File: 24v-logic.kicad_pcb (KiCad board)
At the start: 2 copper layers, 56.4 x 78.7 mm, 55 parts, among them J1 Conn_02x10_Odd_Even, J2 Screw_Terminal_01x09, J3 Conn_02x10_Odd_Even

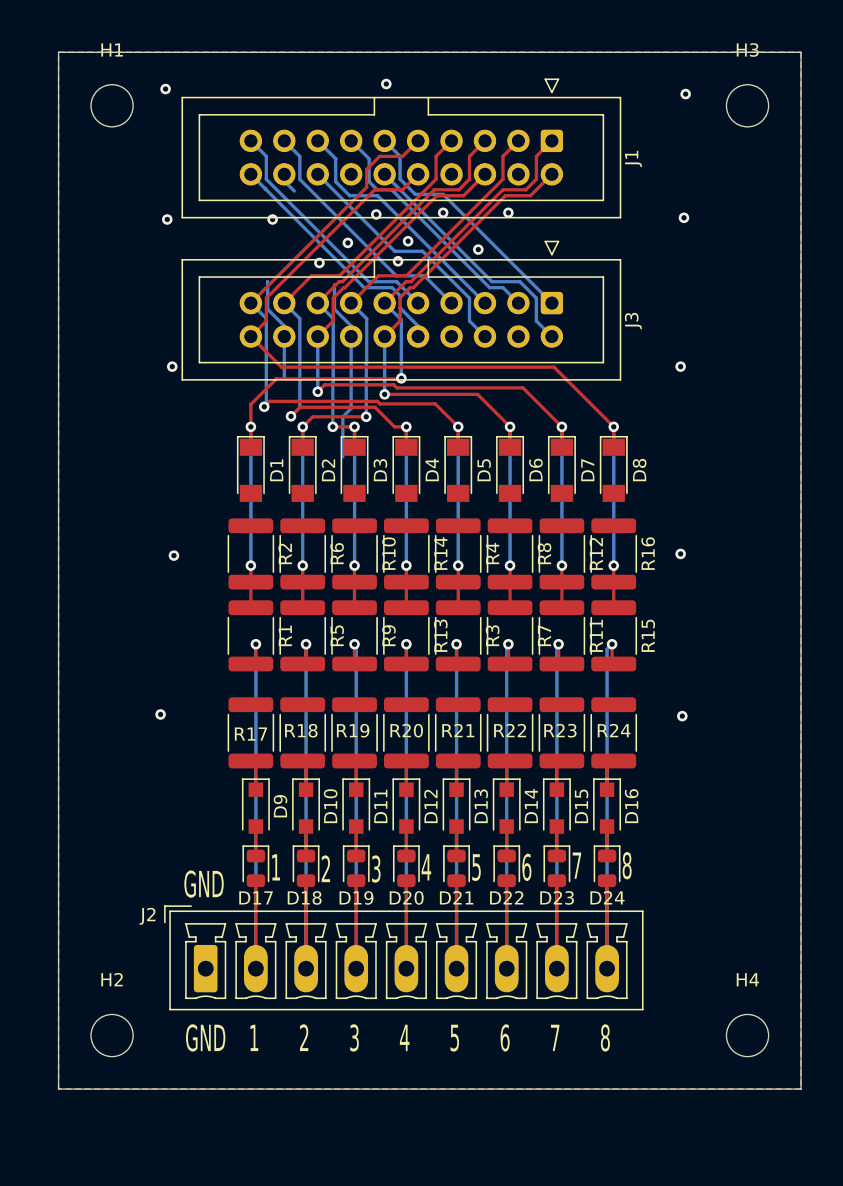
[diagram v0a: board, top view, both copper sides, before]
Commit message: Changes for missing components and migrating to KiCAD 6
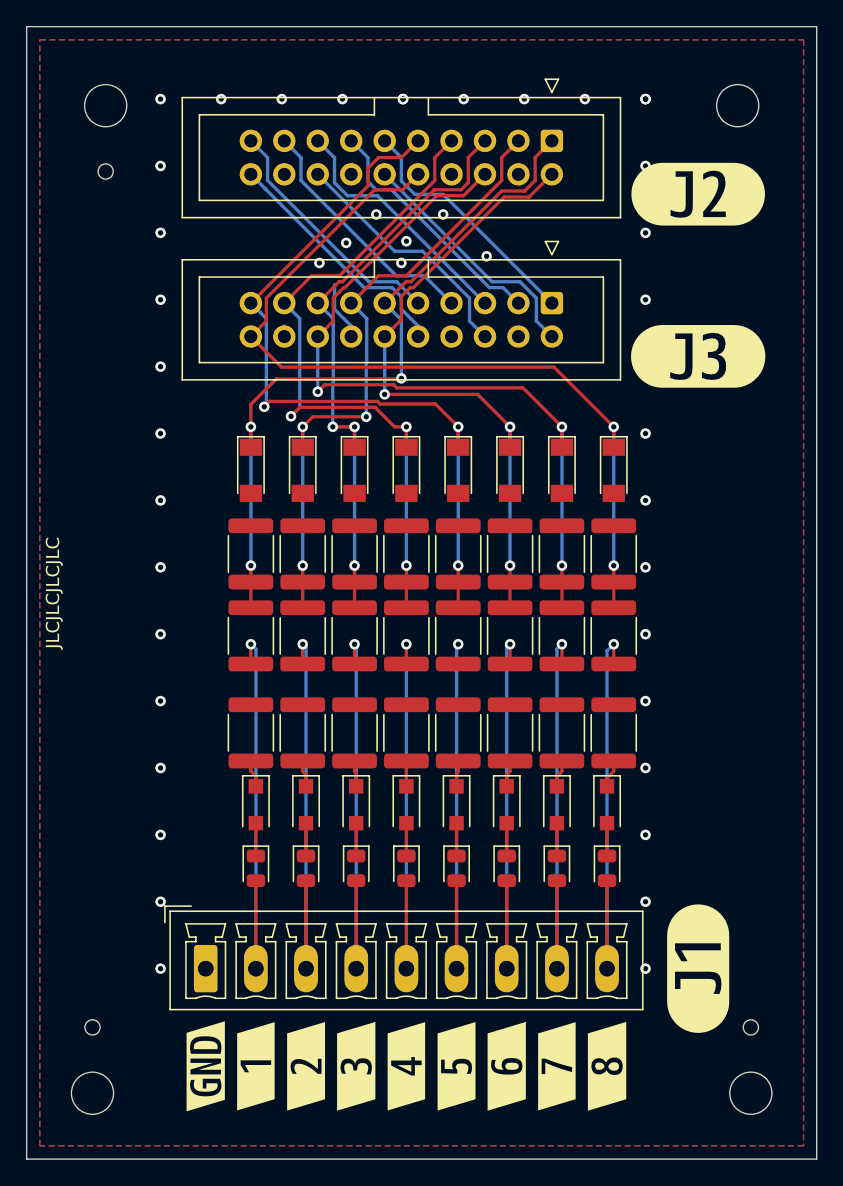
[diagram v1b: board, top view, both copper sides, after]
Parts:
- added REF**: MountingHole_2.1mm, MountingHole:MountingHole_2.1mm, F.Cu at (85.0, 134.0)
- added REF**: MountingHole_2.1mm, MountingHole:MountingHole_2.1mm, F.Cu at (135.0, 134.0)
- added REF**: MountingHole_2.1mm, MountingHole:MountingHole_2.1mm, F.Cu at (86.0, 69.0)
- added kibuzzard-62FC7920: G***, kibuzzard-62FC7920, F.Cu at (93.6, 137.0)
- added kibuzzard-62FC7940: G***, kibuzzard-62FC7940, F.Cu at (101.2, 137.0)
- added kibuzzard-62FC794D: G***, kibuzzard-62FC794D, F.Cu at (97.4, 137.0)
- added kibuzzard-62FC7992: G***, kibuzzard-62FC7992, F.Cu at (105.0, 137.0)
- added kibuzzard-62FC799A: G***, kibuzzard-62FC799A, F.Cu at (108.8, 137.0)
- added kibuzzard-62FC79A9: G***, kibuzzard-62FC79A9, F.Cu at (112.6, 137.0)
- added kibuzzard-62FC79AF: G***, kibuzzard-62FC79AF, F.Cu at (116.5, 137.0)
- added kibuzzard-62FC79B6: G***, kibuzzard-62FC79B6, F.Cu at (120.3, 137.0)
- added kibuzzard-62FC79BD: G***, kibuzzard-62FC79BD, F.Cu at (124.1, 137.0)
- added kibuzzard-62FC7CD0: G***, kibuzzard-62FC7CD0, F.Cu at (131.0, 129.5)
- added kibuzzard-62FC7D50: G***, kibuzzard-62FC7D50, F.Cu at (131.0, 83.0)
- added kibuzzard-62FC7D6D: G***, kibuzzard-62FC7D6D, F.Cu at (131.0, 70.7)
- D1, D3, D5, D7: value 5,6V -> D; footprint Diode_SMD:D_MiniMELF -> Diode_SMD:D_SOD-123F
- D10, D11, D14, D16: value D -> R; footprint Diode_SMD:D_SOD-123F -> Diode_SMD:D_0805_2012Metric
- D17, D18, D19, D20, D21, D22, D23, D24: value R -> 5,6V; footprint Diode_SMD:D_0805_2012Metric -> Diode_SMD:D_MiniMELF
- D2, D4, D6, D8: value 5,6V -> R; footprint Diode_SMD:D_MiniMELF -> Diode_SMD:D_0805_2012Metric
- R1, R19, R22, R5: value 3800 -> 1k
- R10, R14, R16, R2: value 1000 -> 1k
- R11, R13, R15, R17, R18, R20, R21, R23, R24, R3, R7, R9: value 3800 -> 3.9k
- R12, R4, R6, R8: value 1000 -> 3.9k
- moved D8 36.0 mm to (105.0, 121.9)
- moved D21 34.0 mm to (97.0, 91.7)
- moved D22 31.3 mm to (124.6, 91.7)
- moved D6 31.2 mm to (108.8, 121.9)
- moved D20 30.5 mm to (112.8, 91.7)
- moved D19 30.5 mm to (108.8, 91.7)
- moved D4 30.5 mm to (112.6, 121.9)
- moved D18 30.4 mm to (104.9, 91.7)
- moved D17 30.4 mm to (101.0, 91.7)
- moved D23 30.4 mm to (116.7, 91.7)
- moved D24 30.4 mm to (120.7, 91.7)
- moved D2 30.2 mm to (101.2, 121.9)
- moved D7 29.8 mm to (105.0, 117.1)
- moved R17 27.6 mm to (124.6, 111.6)
- moved R12 27.3 mm to (97.0, 111.6)
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- renumbered H2 to H1, H4 to H2, H1 to H3, H3 to H4, J2 to J1, J1 to J2
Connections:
- D1 pad 1: D0 -> Net-(D8-Pad1)
- D1 pad 2: GND -> Net-(D7-Pad1)
- D10 pad 1: Net-(D10-Pad1) -> Net-(D1-Pad1)
- D10 pad 2: Net-(D10-Pad2) -> I24-0
- D11 pad 1: Net-(D11-Pad1) -> Net-(D19-Pad1)
- D11 pad 2: Net-(D11-Pad2) -> I24-5
- D12 pad 2: Net-(D12-Pad2) -> Net-(D19-Pad1)
- D13 pad 1: Net-(D13-Pad1) -> Net-(D5-Pad1)
- D13 pad 2: Net-(D13-Pad2) -> Net-(D4-Pad1)
- D14 pad 1: Net-(D14-Pad1) -> Net-(D22-Pad1)
- D14 pad 2: Net-(D14-Pad2) -> I24-6
- D15 pad 2: Net-(D15-Pad2) -> Net-(D22-Pad1)
- D16 pad 1: Net-(D16-Pad1) -> Net-(D4-Pad1)
- D16 pad 2: Net-(D16-Pad2) -> I24-7
- D17 pad 1: Net-(D17-Pad1) -> D1
- D17 pad 2: I24-0 -> GND
- D18 pad 1: Net-(D10-Pad2) -> D2
- D18 pad 2: I24-1 -> GND
- D19 pad 1: Net-(D11-Pad2) -> D3
- D19 pad 2: I24-2 -> GND
- D2 pad 1: D1 -> Net-(D7-Pad1)
- D2 pad 2: GND -> I24-1
- D20 pad 1: Net-(D12-Pad2) -> D4
- D20 pad 2: I24-3 -> GND
- D21 pad 1: Net-(D13-Pad2) -> D0
- D21 pad 2: I24-4 -> GND
- D22 pad 1: Net-(D14-Pad2) -> D7
- D22 pad 2: I24-5 -> GND
- D23 pad 1: Net-(D15-Pad2) -> D5
- D23 pad 2: I24-6 -> GND
- D24 pad 1: Net-(D16-Pad2) -> D6
- D24 pad 2: I24-7 -> GND
- D3 pad 1: D2 -> Net-(D17-Pad1)
- D3 pad 2: GND -> Net-(D16-Pad1)
- D4 pad 1: D3 -> Net-(D16-Pad1)
- D4 pad 2: GND -> I24-4
- D5 pad 1: D4 -> Net-(D14-Pad1)
- D5 pad 2: GND -> Net-(D13-Pad1)
- D6 pad 1: D5 -> Net-(D13-Pad1)
- D6 pad 2: GND -> I24-3
- D7 pad 1: D6 -> Net-(D11-Pad1)
- D7 pad 2: GND -> Net-(D10-Pad1)
- D8 pad 1: D7 -> Net-(D10-Pad1)
- D8 pad 2: GND -> I24-2
- D9 pad 1: Net-(D9-Pad1) -> Net-(D2-Pad1)
- D9 pad 2: Net-(D17-Pad1) -> Net-(D1-Pad1)
- R1 pad 1: D0 -> GND
- R1 pad 2: I24-0 -> D2
- R10 pad 2: D2 -> D1
- R11 pad 1: D6 -> D1
- R11 pad 2: I24-6 -> I24-1
- R12 pad 2: D6 -> Net-(D2-Pad1)
- R13 pad 1: D3 -> D0
- R13 pad 2: I24-3 -> I24-0
- R14 pad 2: D3 -> D0
- R15 pad 1: D7 -> GND
- R15 pad 2: I24-7 -> Net-(D8-Pad1)
- R16 pad 2: D7 -> D6
- R17 pad 2: Net-(D9-Pad1) -> Net-(D5-Pad1)
- R18 pad 1: GND -> D7
- R18 pad 2: Net-(D10-Pad1) -> I24-7
- R19 pad 2: Net-(D11-Pad1) -> D7
- R2 pad 2: D0 -> D4
- R21 pad 1: GND -> D5
- R21 pad 2: Net-(D13-Pad1) -> I24-5
- R22 pad 2: Net-(D14-Pad1) -> D5
- R24 pad 1: GND -> D6
- R24 pad 2: Net-(D16-Pad1) -> I24-6
- R4 pad 2: D4 -> Net-(D17-Pad1)
- R5 pad 1: D1 -> GND
- R5 pad 2: I24-1 -> D3
- R6 pad 1: GND -> D3
- R6 pad 2: D1 -> I24-3
- R7 pad 1: D5 -> GND
- R7 pad 2: I24-5 -> Net-(D14-Pad1)
- R8 pad 1: GND -> D2
- R8 pad 2: D5 -> I24-2
- R9 pad 1: D2 -> GND
- R9 pad 2: I24-2 -> Net-(D11-Pad1)
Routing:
- net GND: track 23.3 -> 5.77 mm, vias 20 -> 7
- net Net-(D7-Pad1): track 0.00 -> 2.49 mm
- net Net-(D4-Pad1): track 0.00 -> 2.49 mm
- net Net-(D22-Pad1): track 0.00 -> 2.49 mm
- net Net-(D19-Pad1): track 0.00 -> 2.49 mm
- net Net-(D1-Pad1): track 0.00 -> 2.49 mm
- net Net-(D9-Pad1): track 2.34 -> 0.00 mm
- net Net-(D16-Pad2): track 2.23 -> 0.00 mm
- net Net-(D15-Pad2): track 2.23 -> 0.00 mm
- net Net-(D14-Pad2): track 2.23 -> 0.00 mm
- net Net-(D13-Pad2): track 2.23 -> 0.00 mm
- net Net-(D12-Pad2): track 2.23 -> 0.00 mm
- net Net-(D11-Pad2): track 2.23 -> 0.00 mm
- net Net-(D10-Pad2): track 2.23 -> 0.00 mm
- net Net-(D5-Pad1): track 0.00 -> 2.13 mm
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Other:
- board size 56.4 x 78.7 mm -> 60 x 86 mm
- rule pad_to_mask_clearance: 0.05 -> 0
- board text added: "JLCJLCJLCJLC"
- board text removed: "1"
- board text removed: "2"
- board text removed: "3"
- board text removed: "4"
- board text removed: "5"
- board text removed: "6"
- board text removed: "7"
- board text removed: "8"
- board text removed: "GND"
